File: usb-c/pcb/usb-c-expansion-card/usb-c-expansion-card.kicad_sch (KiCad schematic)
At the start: 0 parts

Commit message: Schematic Diagram electrically finished
Signed-off-by: Lucy <user@domain.tld>
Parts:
- added D1, D2, D3, D4, D5, D6, D7, D8: AZ5B0S-01F, Diode_SMD:D_0603_1608Metric, symbol Device:D_TVS
- added J1: USB_C_Receptacle, Connector_USB:USB_C_Receptacle_Molex_105450-0101, symbol Connector:USB_C_Receptacle
- added P1: USB_C_Plug, Expansion_Card:USB_C_Plug_Molex_105444, symbol Connector:USB_C_Plug
- added U1, U2, U3: USBLC6-2SC6, Package_TO_SOT_SMD:SOT-23-6, symbol Power_Protection:USBLC6-2SC6
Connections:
- new net: P1.A5 (CC), U3.6 (I/O1)
- new net: P1.A6 (D+), U1.4 (I/O2)
- new net: P1.A7 (D-), U1.6 (I/O1)
- new net: P1.A8 (SBU1), U2.6 (I/O1)
- new net: P1.B5 (VCONN), U3.4 (I/O2)
- new net: P1.B8 (SBU2), U2.4 (I/O2)
- new net: J1.A5 (CC1), U3.1 (I/O1)
- new net: J1.B5 (CC2), U3.3 (I/O2)
- new net: J1.A7 (D-), J1.B7 (D-), U1.1 (I/O1)
- new net: J1.A6 (D+), J1.B6 (D+), U1.3 (I/O2)
- new net: J1.A8 (SBU1), U2.1 (I/O1)
- new net: J1.B8 (SBU2), U2.3 (I/O2)
- new net GND: D1.2 (A2), D2.2 (A2), D3.2 (A2), D4.2 (A2), D5.2 (A2), D6.2 (A2), D7.2 (A2), D8.2 (A2), J1.A1 (GND), J1.A12 (GND), J1.B1 (GND), J1.B12 (GND), J1.SH (SHIELD), P1.A1 (GND), P1.A12 (GND), P1.B1 (GND), P1.B12 (GND), P1.SH (SHIELD), U1.2 (GND), U2.2 (GND), U3.2 (GND)
- new net RX1N_ESD: D1.1 (A1), J1.B10 (RX1-), P1.B10 (RX1-)
- new net RX1P_ESD: D2.1 (A1), J1.B11 (RX1+), P1.B11 (RX1+)
- new net RX2N_ESD: D5.1 (A1), J1.A10 (RX2-), P1.A10 (RX2-)
- new net RX2P_ESD: D6.1 (A1), J1.A11 (RX2+), P1.A11 (RX2+)
- new net TX1N_ESD: D3.1 (A1), J1.A3 (TX1-), P1.A3 (TX1-)
- new net TX1P_ESD: D4.1 (A1), J1.A2 (TX1+), P1.A2 (TX1+)
- new net TX2N_ESD: D7.1 (A1), J1.B3 (TX2-), P1.B3 (TX2-)
- new net TX2P_ESD: D8.1 (A1), J1.B2 (TX2+), P1.B2 (TX2+)
- new net VBUS: J1.A4 (VBUS), J1.A9 (VBUS), J1.B4 (VBUS), J1.B9 (VBUS), P1.A4 (VBUS), P1.A9 (VBUS), P1.B4 (VBUS), P1.B9 (VBUS)
- no-connect marks 0 -> 2
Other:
- company: (none) -> ${COMPANY}
- title: (none) -> ${TITLE}

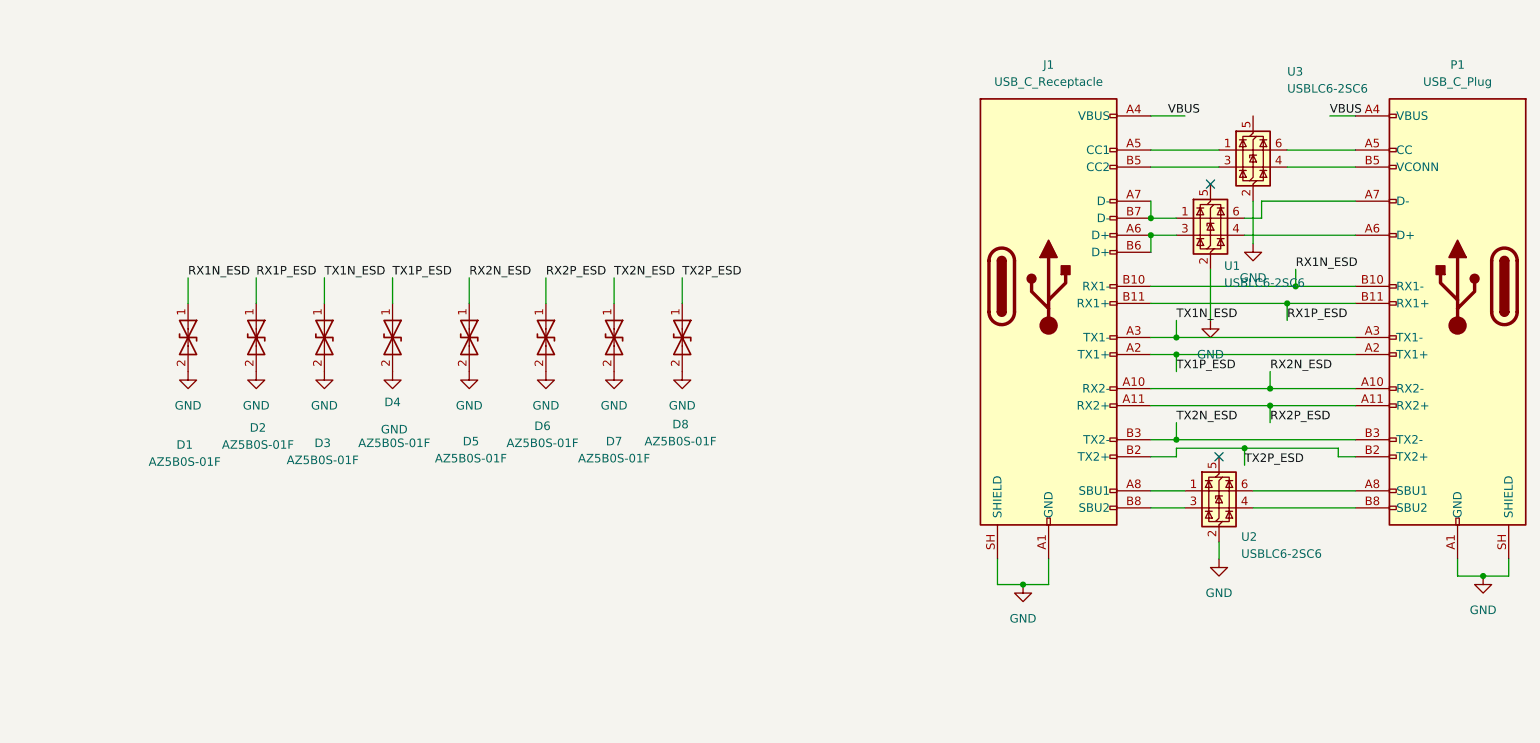
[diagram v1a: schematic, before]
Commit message: Begin routing PCB
Signed-off-by: Lucy <user@domain.tld>
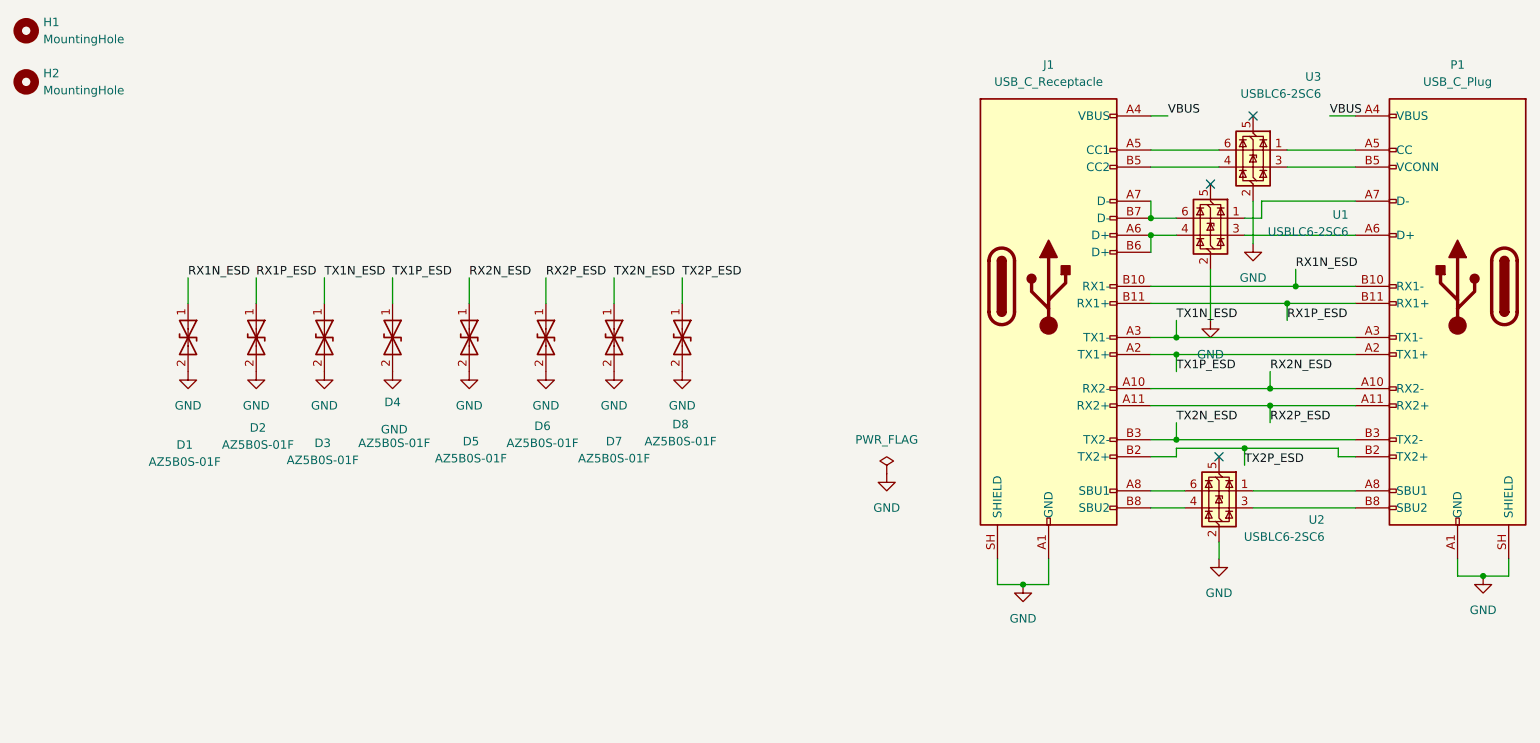
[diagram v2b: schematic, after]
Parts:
- added H1, H2: MountingHole, MountingHole:MountingHole_2.2mm_M2_DIN965_Pad, symbol Mechanical:MountingHole
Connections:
- net at P1.A5 (CC): now also U3.1 (I/O1); no longer U3.6 (I/O1)
- net at P1.A6 (D+): now also U1.3 (I/O2); no longer U1.4 (I/O2)
- net at P1.A7 (D-): now also U1.1 (I/O1); no longer U1.6 (I/O1)
- net at P1.A8 (SBU1): now also U2.1 (I/O1); no longer U2.6 (I/O1)
- net at P1.B5 (VCONN): now also U3.3 (I/O2); no longer U3.4 (I/O2)
- net at P1.B8 (SBU2): now also U2.3 (I/O2); no longer U2.4 (I/O2)
- net at J1.A5 (CC1): now also U3.6 (I/O1); no longer U3.1 (I/O1)
- net at J1.B5 (CC2): now also U3.4 (I/O2); no longer U3.3 (I/O2)
- net at J1.A7 (D-), J1.B7 (D-): now also U1.6 (I/O1); no longer U1.1 (I/O1)
- net at J1.A6 (D+), J1.B6 (D+): now also U1.4 (I/O2); no longer U1.3 (I/O2)
- net at J1.A8 (SBU1): now also U2.6 (I/O1); no longer U2.1 (I/O1)
- net at J1.B8 (SBU2): now also U2.4 (I/O2); no longer U2.3 (I/O2)
- no-connect marks 2 -> 3

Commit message: Update net labels for differential pair routing
Signed-off-by: Lucy <user@domain.tld>
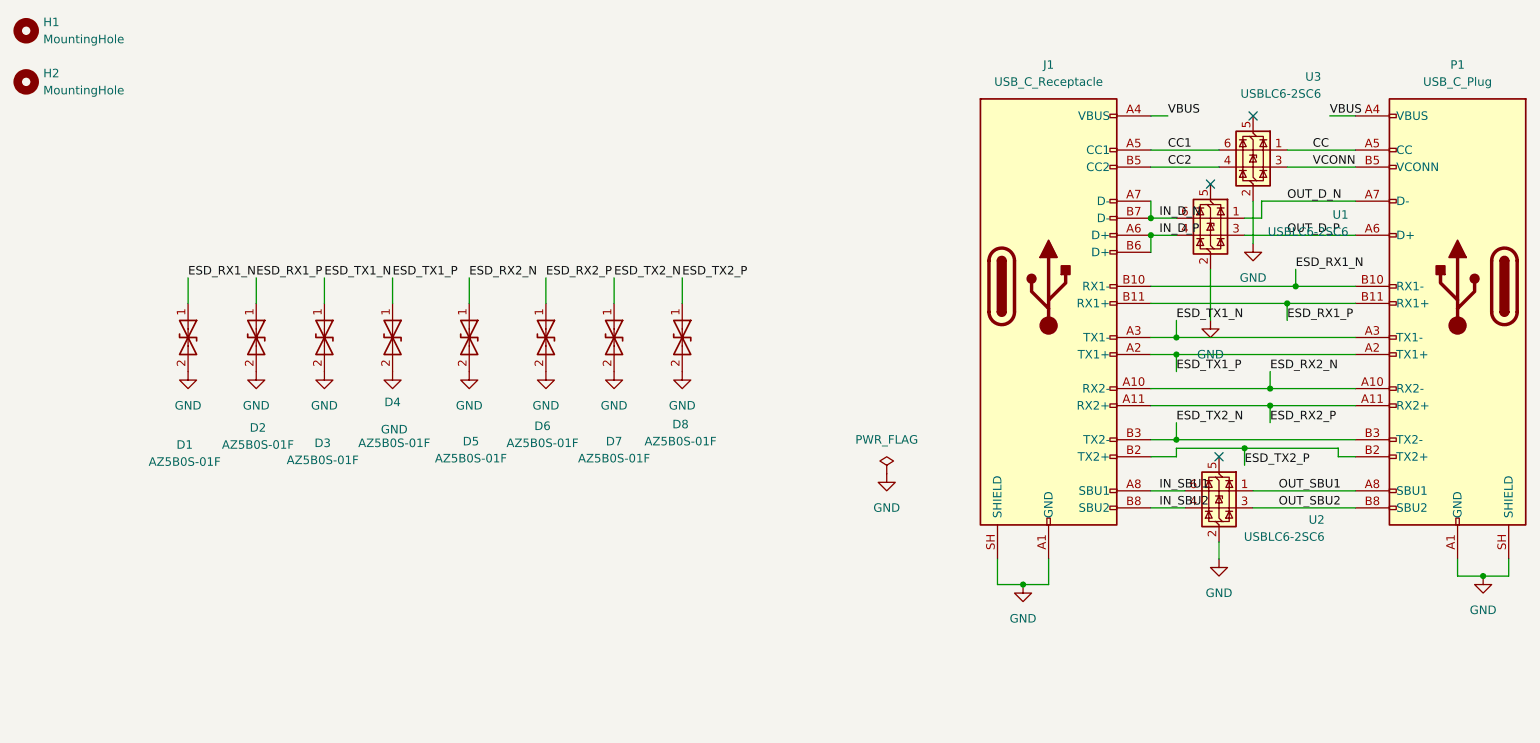
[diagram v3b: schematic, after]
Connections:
- net CC: now reaches P1.A5 (CC), U3.1 (I/O1)
- net OUT_D_P: now reaches P1.A6 (D+), U1.3 (I/O2)
- net OUT_D_N: now reaches P1.A7 (D-), U1.1 (I/O1)
- net OUT_SBU1: now reaches P1.A8 (SBU1), U2.1 (I/O1)
- net VCONN: now reaches P1.B5 (VCONN), U3.3 (I/O2)
- net OUT_SBU2: now reaches P1.B8 (SBU2), U2.3 (I/O2)
- net CC2: now reaches J1.B5 (CC2), U3.4 (I/O2)
- net CC1: now reaches J1.A5 (CC1), U3.6 (I/O1)
- net IN_D_P: now reaches J1.A6 (D+), J1.B6 (D+), U1.4 (I/O2)
- net IN_D_N: now reaches J1.A7 (D-), J1.B7 (D-), U1.6 (I/O1)
- net IN_SBU1: now reaches J1.A8 (SBU1), U2.6 (I/O1)
- net IN_SBU2: now reaches J1.B8 (SBU2), U2.4 (I/O2)
- net RX1N_ESD renamed ESD_RX1_N
- net RX1P_ESD renamed ESD_RX1_P
- net RX2N_ESD renamed ESD_RX2_N
- net RX2P_ESD renamed ESD_RX2_P
- net TX1N_ESD renamed ESD_TX1_N
- net TX1P_ESD renamed ESD_TX1_P
- net TX2N_ESD renamed ESD_TX2_N
- net TX2P_ESD renamed ESD_TX2_P
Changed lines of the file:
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@@
 		)
 	)
-	(label "TX2P_ESD"
+	(label "ESD_TX2_P"
 		(at 128.27 60.96 0)
 		(effects
@@
 		)
 	)
-	(label "TX2N_ESD"
+	(label "ESD_TX2_N"
 		(at 118.11 60.96 0)
+		(effects
+			(font
+				(size 1.27 1.27)
+			)
+			(justify left bottom)
+		)
+	)
+	(label "VCONN"
+		(at 222.25 44.45 0)
+		(effects
+			(font
+				(size 1.27 1.27)
+			)
+			(justify left bottom)
+		)
+	)
+	(label "IN_SBU2"
+		(at 199.39 95.25 0)
 		(effects
 			(font
@@
 		)
 	)
-	(label "RX2P_ESD"
+	(label "ESD_RX2_P"
 		(at 107.95 60.96 0)
 		(effects
@@
 		)
 	)
-	(label "TX1P_ESD"
+	(label "ESD_TX1_P"
 		(at 201.93 74.93 0)
 		(effects
@@
 		)
 	)
-	(label "RX2N_ESD"
+	(label "ESD_RX2_N"
 		(at 96.52 60.96 0)
 		(effects
@@
 		)
 	)
-	(label "RX1P_ESD"
+	(label "ESD_RX1_P"
 		(at 64.77 60.96 0)
 		(effects
@@
 		)
 	)
-	(label "TX2N_ESD"
+	(label "ESD_TX2_N"
 		(at 201.93 82.55 0)
 		(effects
@@
 		)
 	)
-	(label "RX1P_ESD"
+	(label "ESD_RX1_P"
 		(at 218.44 67.31 0)
 		(effects
@@
 		)
 	)
-	(label "RX2P_ESD"
+	(label "ESD_RX2_P"
 		(at 215.9 82.55 0)
 		(effects
@@
 		)
 	)
-	(label "TX1P_ESD"
+	(label "OUT_SBU1"
+		(at 217.17 92.71 0)
+		(effects
+			(font
+				(size 1.27 1.27)
+			)
+			(justify left bottom)
+		)
+	)
+	(label "CC1"
+		(at 200.66 41.91 0)
+		(effects
+			(font
+				(size 1.27 1.27)
+			)
+			(justify left bottom)
+		)
+	)
+	(label "ESD_TX1_P"
 		(at 85.09 60.96 0)
 		(effects
@@
 		)
 	)
-	(label "RX2N_ESD"
+	(label "CC"
+		(at 222.25 41.91 0)
+		(effects
+			(font
+				(size 1.27 1.27)
+			)
+			(justify left bottom)
+		)
+	)
+	(label "CC2"
+		(at 200.66 44.45 0)
+		(effects
+			(font
+				(size 1.27 1.27)
+			)
+			(justify left bottom)
+		)
+	)
+	(label "ESD_RX2_N"
 		(at 215.9 74.93 0)
 		(effects
@@
 		)
 	)
-	(label "TX1N_ESD"
+	(label "OUT_D_P"
+		(at 218.44 54.61 0)
+		(effects
+			(font
+				(size 1.27 1.27)
+			)
+			(justify left bottom)
+		)
+	)
+	(label "ESD_TX1_N"
 		(at 201.93 67.31 0)
 		(effects
@@
 		)
 	)
-	(label "TX1N_ESD"
+	(label "IN_SBU1"
+		(at 199.39 92.71 0)
+		(effects
+			(font
+				(size 1.27 1.27)
+			)
+			(justify left bottom)
+		)
+	)
+	(label "OUT_SBU2"
+		(at 217.17 95.25 0)
+		(effects
+			(font
+				(size 1.27 1.27)
+			)
+			(justify left bottom)
+		)
+	)
+	(label "ESD_TX1_N"
 		(at 74.93 60.96 0)
 		(effects
@@
 		)
 	)
-	(label "RX1N_ESD"
+	(label "ESD_RX1_N"
 		(at 219.71 59.69 0)
 		(effects
@@
 		)
 	)
-	(label "RX1N_ESD"
+	(label "OUT_D_N"
+		(at 218.44 49.53 0)
+		(effects
+			(font
+				(size 1.27 1.27)
+			)
+			(justify left bottom)
+		)
+	)
+	(label "IN_D_P"
+		(at 199.39 54.61 0)
+		(effects
+			(font
+				(size 1.27 1.27)
+			)
+			(justify left bottom)
+		)
+	)
+	(label "ESD_RX1_N"
 		(at 54.61 60.96 0)
 		(effects
@@
 		)
 	)
-	(label "TX2P_ESD"
+	(label "IN_D_N"
+		(at 199.39 52.07 0)
+		(effects
+			(font
+				(size 1.27 1.27)
+			)
+			(justify left bottom)
+		)
+	)
+	(label "ESD_TX2_P"
 		(at 212.09 88.9 0)
 		(effects

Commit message: first routing w/o ground planes finished
Signed-off-by: Lucy <user@domain.tld>
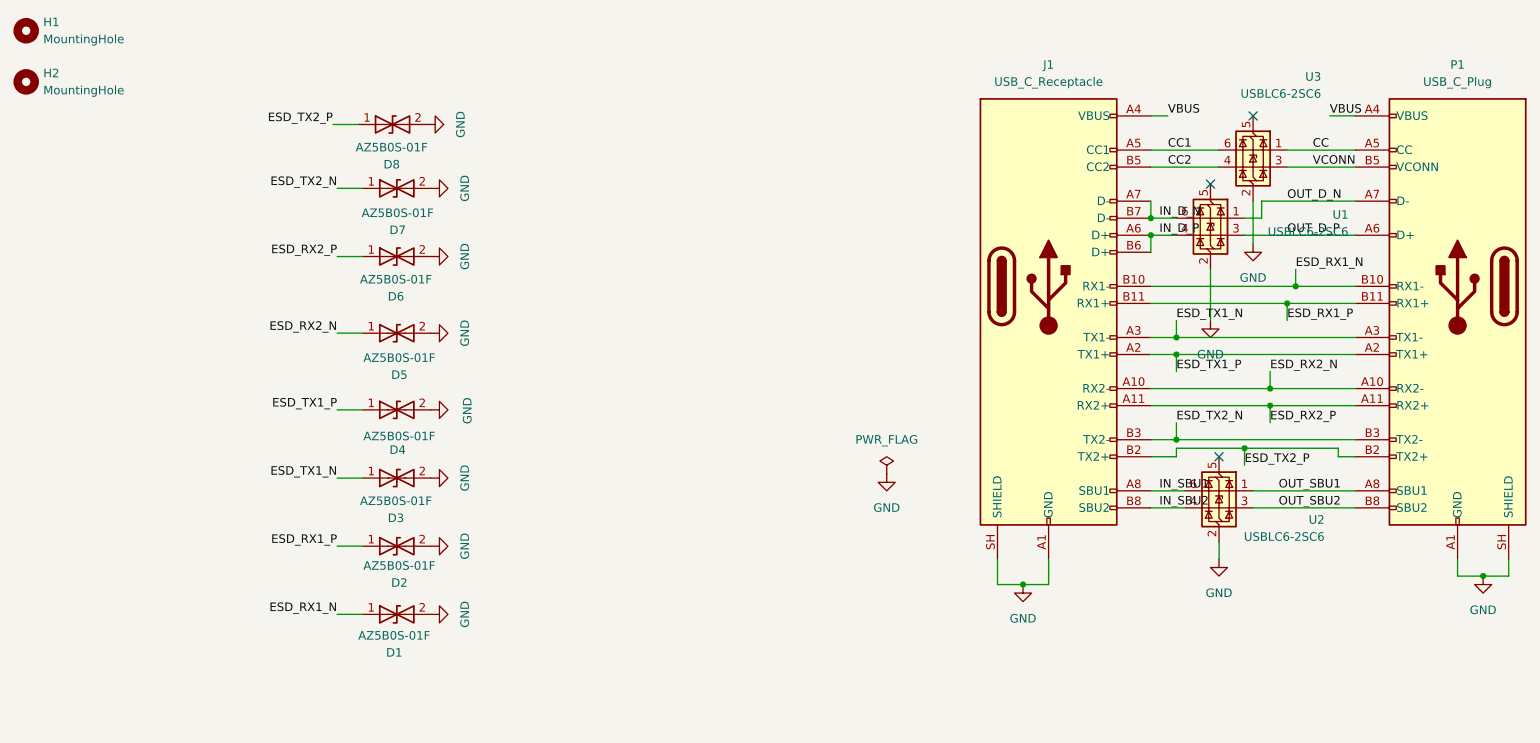
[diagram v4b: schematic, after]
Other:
- moved on the sheet: D1, D2, D3, D4, D5, D6, D7, D8

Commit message: Make schematic more readable
Signed-off-by: Lucy <user@domain.tld>
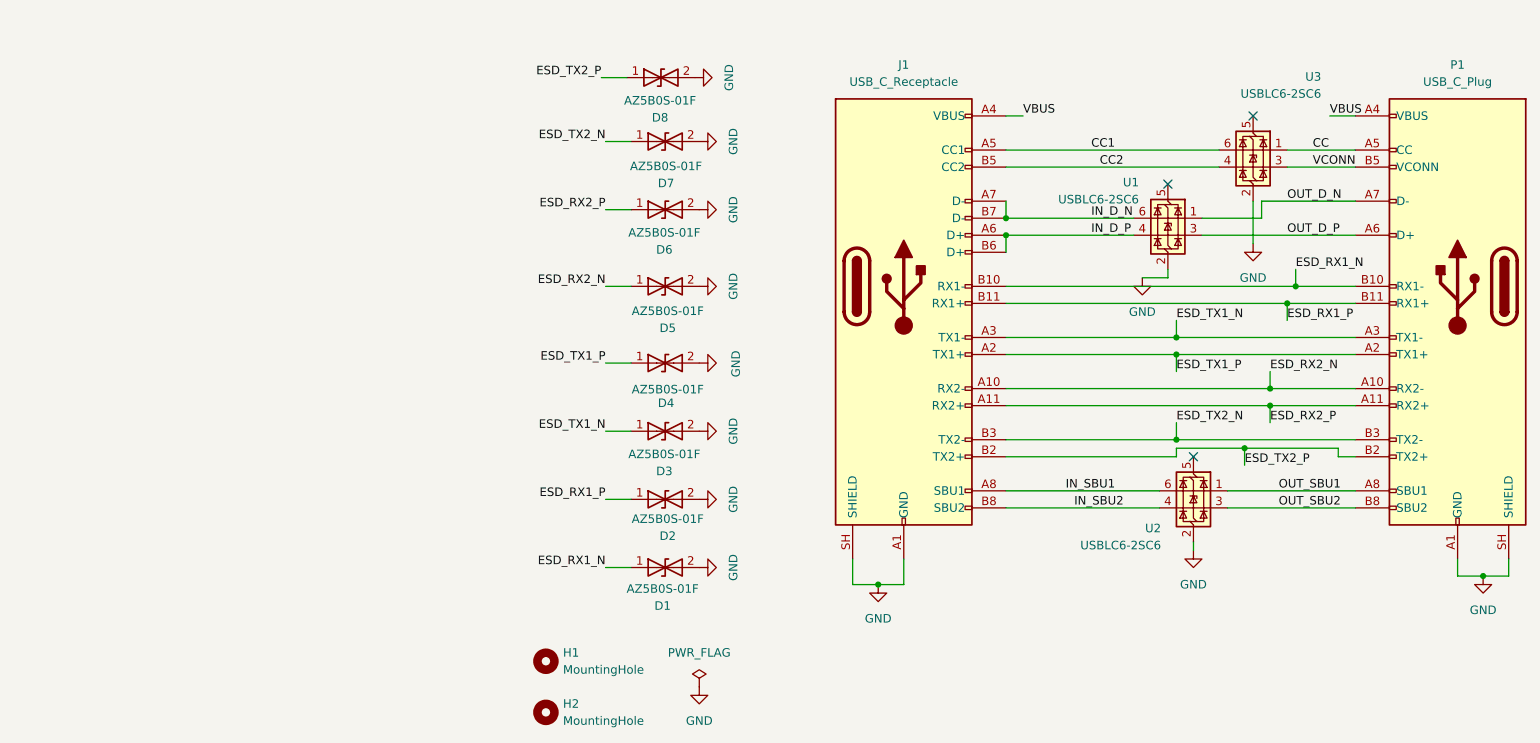
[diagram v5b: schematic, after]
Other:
- moved on the sheet: D1, D2, D3, D4, D5, D6, D7, D8, H1, H2, J1, U1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

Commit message: prepare for partial rewire for better USB-C receptacle footprint
Signed-off-by: Lucy <user@domain.tld>
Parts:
- J1: footprint Connector_USB:USB_C_Receptacle_Molex_105450-0101 -> AMPHENOL-12402075E512A:AMPHENOL_12402075E512A
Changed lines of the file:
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@@
 			)
 		)
-		(property "Footprint" "Connector_USB:USB_C_Receptacle_Molex_105450-0101"
+		(property "Footprint" "AMPHENOL-12402075E512A:AMPHENOL_12402075E512A"
 			(at 165.1 62.23 0)
 			(hide yes)
